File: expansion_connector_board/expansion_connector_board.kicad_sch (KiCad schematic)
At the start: 6 parts, among them J1 Conn_01x04, J12 Conn_02x17_Top_Bottom, J13 Conn_01x04, J14 Conn_02x17_Top_Bottom

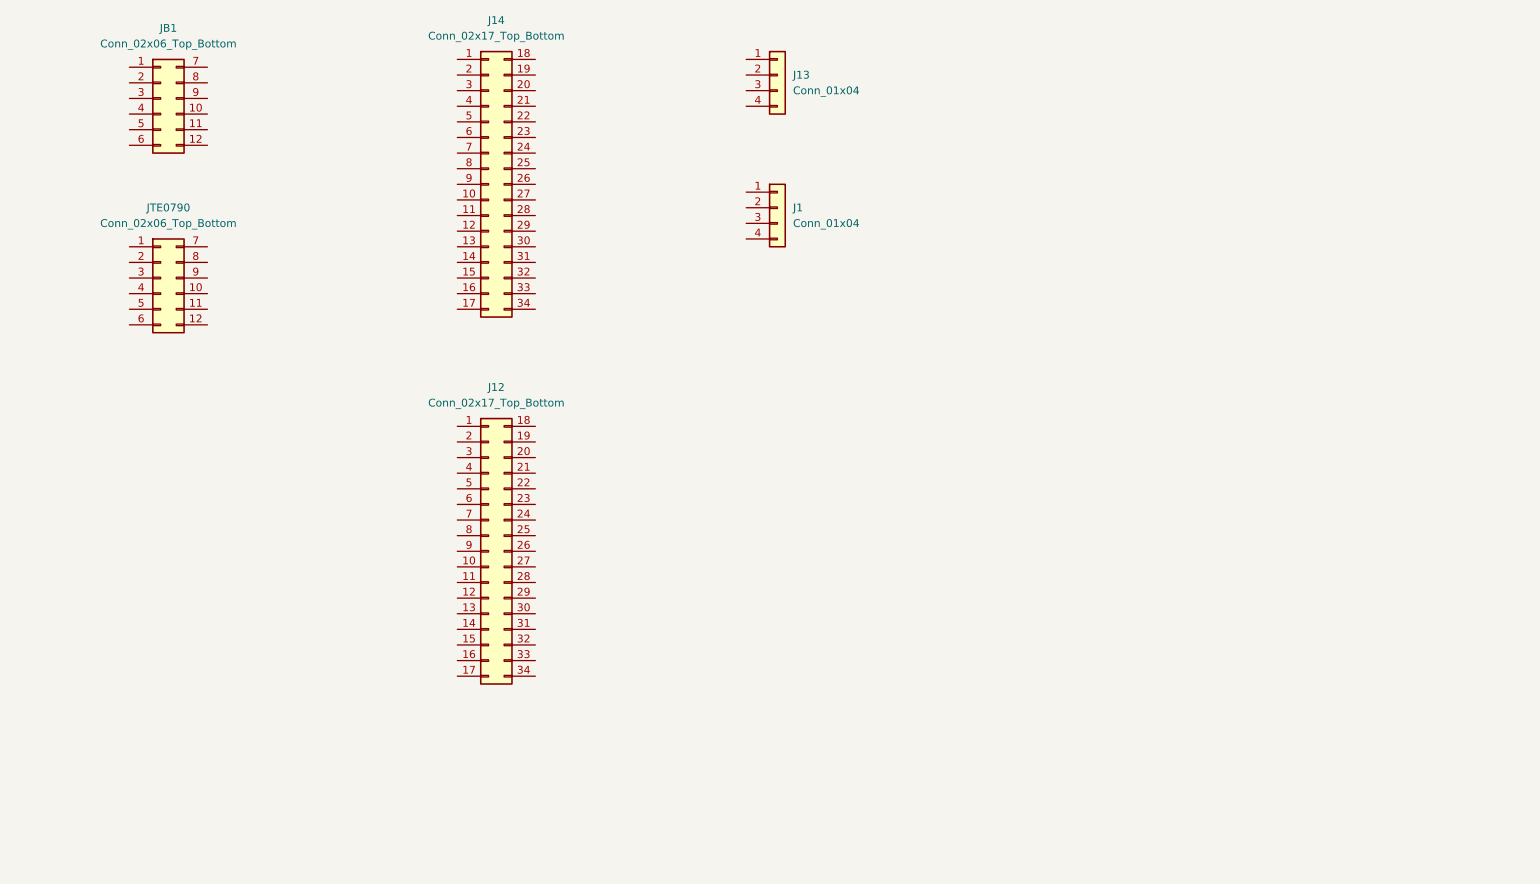
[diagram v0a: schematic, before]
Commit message: complete electrical and cutout of bridge board
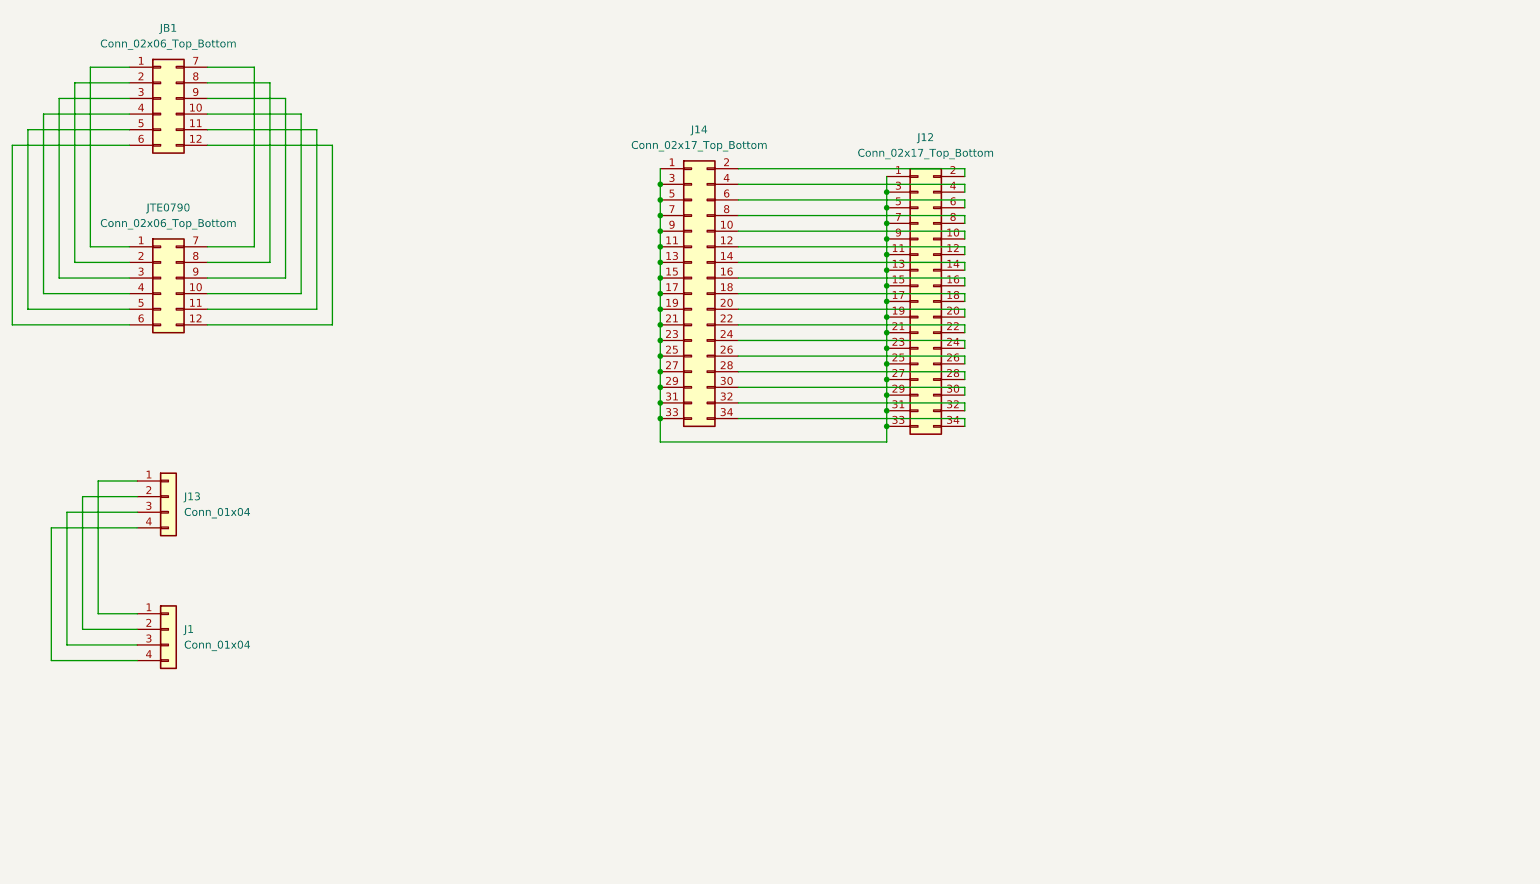
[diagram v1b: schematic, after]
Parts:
- J12, J14: symbol Connector_Generic:Conn_02x17_Top_Bottom -> Connector_Generic:Conn_02x17_Odd_Even
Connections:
- net at J12.1 (Pin_1): now also J12.11 (Pin_11), J12.13 (Pin_13), J12.15 (Pin_15), J12.17 (Pin_17), J12.19 (Pin_19), J12.21 (Pin_21), J12.23 (Pin_23), J12.25 (Pin_25), J12.27 (Pin_27), J12.29 (Pin_29), J12.3 (Pin_3), J12.31 (Pin_31), J12.33 (Pin_33), J12.5 (Pin_5), J12.7 (Pin_7), J12.9 (Pin_9), J14.1 (Pin_1), J14.11 (Pin_11), J14.13 (Pin_13), J14.15 (Pin_15), J14.17 (Pin_17), J14.19 (Pin_19), J14.21 (Pin_21), J14.23 (Pin_23), J14.25 (Pin_25), J14.27 (Pin_27), J14.29 (Pin_29), J14.3 (Pin_3), J14.31 (Pin_31), J14.33 (Pin_33), J14.5 (Pin_5), J14.7 (Pin_7), J14.9 (Pin_9)
- net at J12.10 (Pin_10): now also J14.10 (Pin_10)
- net at J12.12 (Pin_12): now also J14.12 (Pin_12)
- net at J12.14 (Pin_14): now also J14.14 (Pin_14)
- net at J12.16 (Pin_16): now also J14.16 (Pin_16)
- net at J12.18 (Pin_18): now also J14.18 (Pin_18)
- net at J12.2 (Pin_2): now also J14.2 (Pin_2)
- net at J12.20 (Pin_20): now also J14.20 (Pin_20)
- net at J12.22 (Pin_22): now also J14.22 (Pin_22)
- net at J12.24 (Pin_24): now also J14.24 (Pin_24)
- net at J12.26 (Pin_26): now also J14.26 (Pin_26)
- net at J12.28 (Pin_28): now also J14.28 (Pin_28)
- net at J12.30 (Pin_30): now also J14.30 (Pin_30)
- net at J12.32 (Pin_32): now also J14.32 (Pin_32)
- net at J12.34 (Pin_34): now also J14.34 (Pin_34)
- net at J12.4 (Pin_4): now also J14.4 (Pin_4)
- net at J12.6 (Pin_6): now also J14.6 (Pin_6)
- net at J12.8 (Pin_8): now also J14.8 (Pin_8)
- net at JB1.1 (Pin_1): now also JTE0790.1 (Pin_1)
- net at JB1.10 (Pin_10): now also JTE0790.10 (Pin_10)
- net at JB1.11 (Pin_11): now also JTE0790.11 (Pin_11)
- net at JB1.12 (Pin_12): now also JTE0790.12 (Pin_12)
- net at JB1.2 (Pin_2): now also JTE0790.2 (Pin_2)
- net at JB1.3 (Pin_3): now also JTE0790.3 (Pin_3)
- net at JB1.4 (Pin_4): now also JTE0790.4 (Pin_4)
- net at JB1.5 (Pin_5): now also JTE0790.5 (Pin_5)
- net at JB1.6 (Pin_6): now also JTE0790.6 (Pin_6)
- net at JB1.7 (Pin_7): now also JTE0790.7 (Pin_7)
- net at JB1.8 (Pin_8): now also JTE0790.8 (Pin_8)
- net at JB1.9 (Pin_9): now also JTE0790.9 (Pin_9)
- net at J13.1 (Pin_1): now also J1.1 (Pin_1)
- net at J13.2 (Pin_2): now also J1.2 (Pin_2)
- net at J13.3 (Pin_3): now also J1.3 (Pin_3)
- net at J13.4 (Pin_4): now also J1.4 (Pin_4)
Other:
- moved on the sheet: J1, J12, J13, J14

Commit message: trim board size
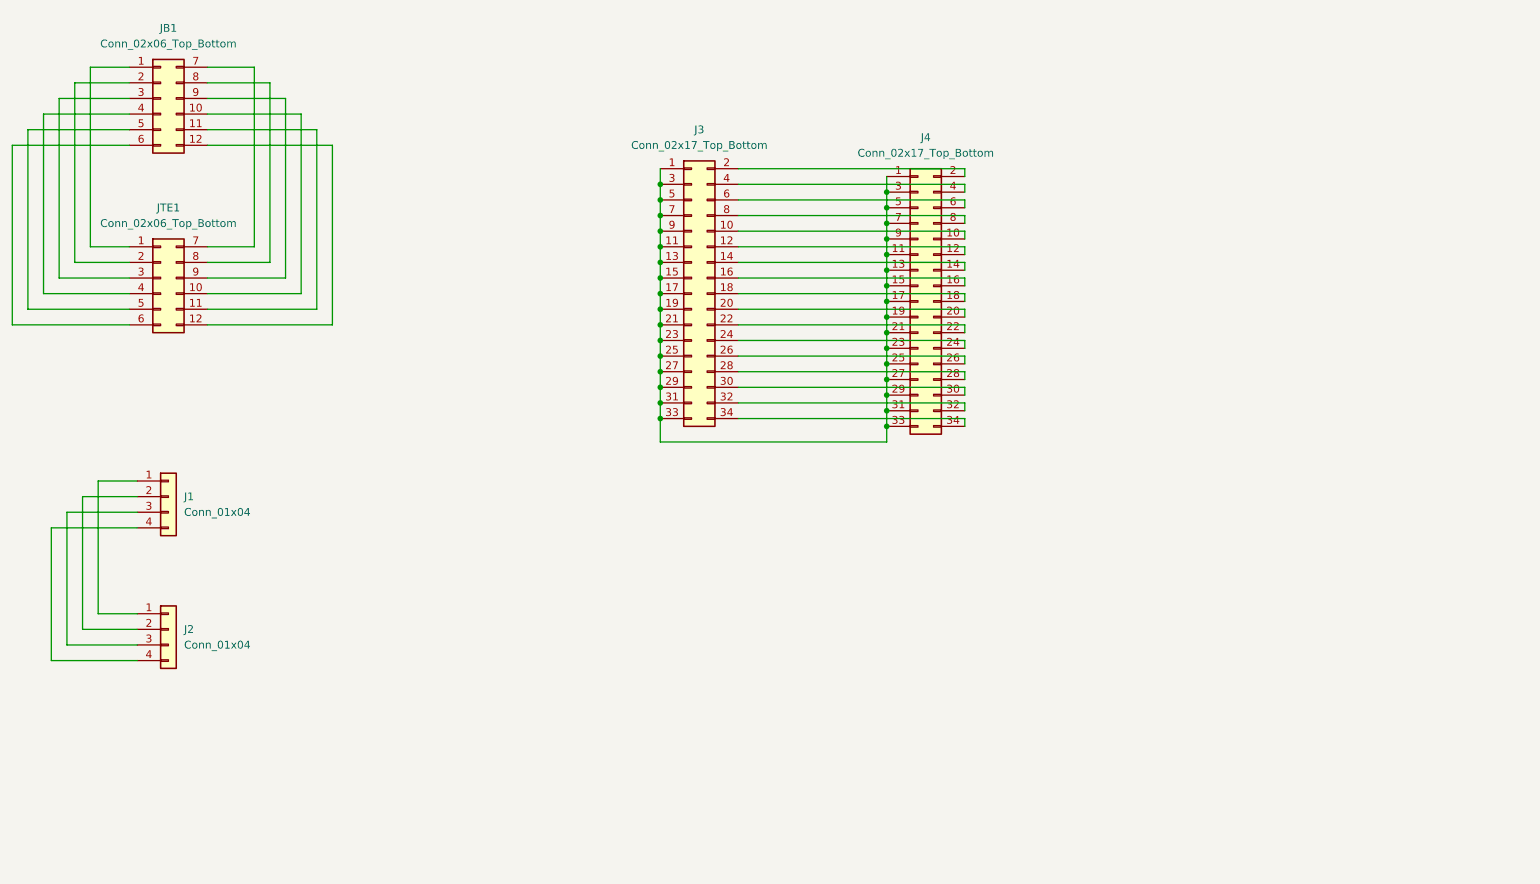
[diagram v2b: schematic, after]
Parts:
- renumbered J13 to J1, J1 to J2, J14 to J3, J12 to J4, JTE0790 to JTE1
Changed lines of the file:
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@@
   (symbol (lib_id "Connector_Generic:Conn_02x17_Odd_Even") (at 170.18 66.04 0) (unit 1)
     (in_bom yes) (on_board yes) (fields_autoplaced)
-    (property "Reference" "J12" (id 0) (at 171.45 39.37 0))
+    (property "Reference" "J4" (id 0) (at 171.45 39.37 0))
     (property "Value" "Conn_02x17_Top_Bottom" (id 1) (at 171.45 41.91 0))
     (property "Footprint" "Connector_PinHeader_2.54mm:PinHeader_2x17_P2.54mm_Vertical" (id 2) (at 170.18 66.04 0)
@@
   (symbol (lib_id "Connector_Generic:Conn_02x17_Odd_Even") (at 133.35 64.77 0) (unit 1)
     (in_bom yes) (on_board yes) (fields_autoplaced)
-    (property "Reference" "J14" (id 0) (at 134.62 38.1 0))
+    (property "Reference" "J3" (id 0) (at 134.62 38.1 0))
     (property "Value" "Conn_02x17_Top_Bottom" (id 1) (at 134.62 40.64 0))
     (property "Footprint" "Connector_PinHeader_2.54mm:PinHeader_2x17_P2.54mm_Vertical" (id 2) (at 133.35 64.77 0)
@@
   (symbol (lib_id "Connector_Generic:Conn_01x04") (at 48.26 97.79 0) (unit 1)
     (in_bom yes) (on_board yes) (fields_autoplaced)
-    (property "Reference" "J13" (id 0) (at 50.8 97.7899 0)
+    (property "Reference" "J1" (id 0) (at 50.8 97.7899 0)
       (effects (font (size 1.27 1.27)) (justify left))
     )
@@
   (symbol (lib_id "Connector_Generic:Conn_01x04") (at 48.26 119.38 0) (unit 1)
     (in_bom yes) (on_board yes) (fields_autoplaced)
-    (property "Reference" "J1" (id 0) (at 50.8 119.3799 0)
+    (property "Reference" "J2" (id 0) (at 50.8 119.3799 0)
       (effects (font (size 1.27 1.27)) (justify left))
     )
@@
   (symbol (lib_id "Connector_Generic:Conn_02x06_Top_Bottom") (at 46.99 62.23 0) (unit 1)
     (in_bom yes) (on_board yes) (fields_autoplaced)
-    (property "Reference" "JTE0790" (id 0) (at 48.26 50.8 0))
+    (property "Reference" "JTE1" (id 0) (at 48.26 50.8 0))
     (property "Value" "Conn_02x06_Top_Bottom" (id 1) (at 48.26 53.34 0))
     (property "Footprint" "Connector_PinHeader_2.54mm:PinHeader_2x06_P2.54mm_Vertical" (id 2) (at 46.99 62.23 0)
@@
   )
   (symbol_instances
-    (path "/ea63a27d-5892-4a4a-b73a-f603e7d18c36"
+    (path "/e081bfea-a76c-4079-8eff-f74da9d0a8b9"
       (reference "J1") (unit 1) (value "Conn_01x04") (footprint "Connector_PinHeader_2.54mm:PinHeader_1x04_P2.54mm_Vertical")
     )
-    (path "/4641dd2b-8a78-420d-8cf9-d253cde42a58"
-      (reference "J12") (unit 1) (value "Conn_02x17_Top_Bottom") (footprint "Connector_PinHeader_2.54mm:PinHeader_2x17_P2.54mm_Vertical")
-    )
-    (path "/e081bfea-a76c-4079-8eff-f74da9d0a8b9"
-      (reference "J13") (unit 1) (value "Conn_01x04") (footprint "Connector_PinHeader_2.54mm:PinHeader_1x04_P2.54mm_Vertical")
+    (path "/ea63a27d-5892-4a4a-b73a-f603e7d18c36"
+      (reference "J2") (unit 1) (value "Conn_01x04") (footprint "Connector_PinHeader_2.54mm:PinHeader_1x04_P2.54mm_Vertical")
     )
     (path "/5e2b1b60-5db0-4075-8d2c-1c593da01486"
-      (reference "J14") (unit 1) (value "Conn_02x17_Top_Bottom") (footprint "Connector_PinHeader_2.54mm:PinHeader_2x17_P2.54mm_Vertical")
+      (reference "J3") (unit 1) (value "Conn_02x17_Top_Bottom") (footprint "Connector_PinHeader_2.54mm:PinHeader_2x17_P2.54mm_Vertical")
+    )
+    (path "/4641dd2b-8a78-420d-8cf9-d253cde42a58"
+      (reference "J4") (unit 1) (value "Conn_02x17_Top_Bottom") (footprint "Connector_PinHeader_2.54mm:PinHeader_2x17_P2.54mm_Vertical")
     )
     (path "/db6f34f2-3650-4262-8a8c-0ff568fe194f"
@@
     )
     (path "/f61065d3-62f3-4952-9f93-3fd8792c420d"
-      (reference "JTE0790") (unit 1) (value "Conn_02x06_Top_Bottom") (footprint "Connector_PinHeader_2.54mm:PinHeader_2x06_P2.54mm_Vertical")
+      (reference "JTE1") (unit 1) (value "Conn_02x06_Top_Bottom") (footprint "Connector_PinHeader_2.54mm:PinHeader_2x06_P2.54mm_Vertical")
     )
   )

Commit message: fix connector placement on bridge board
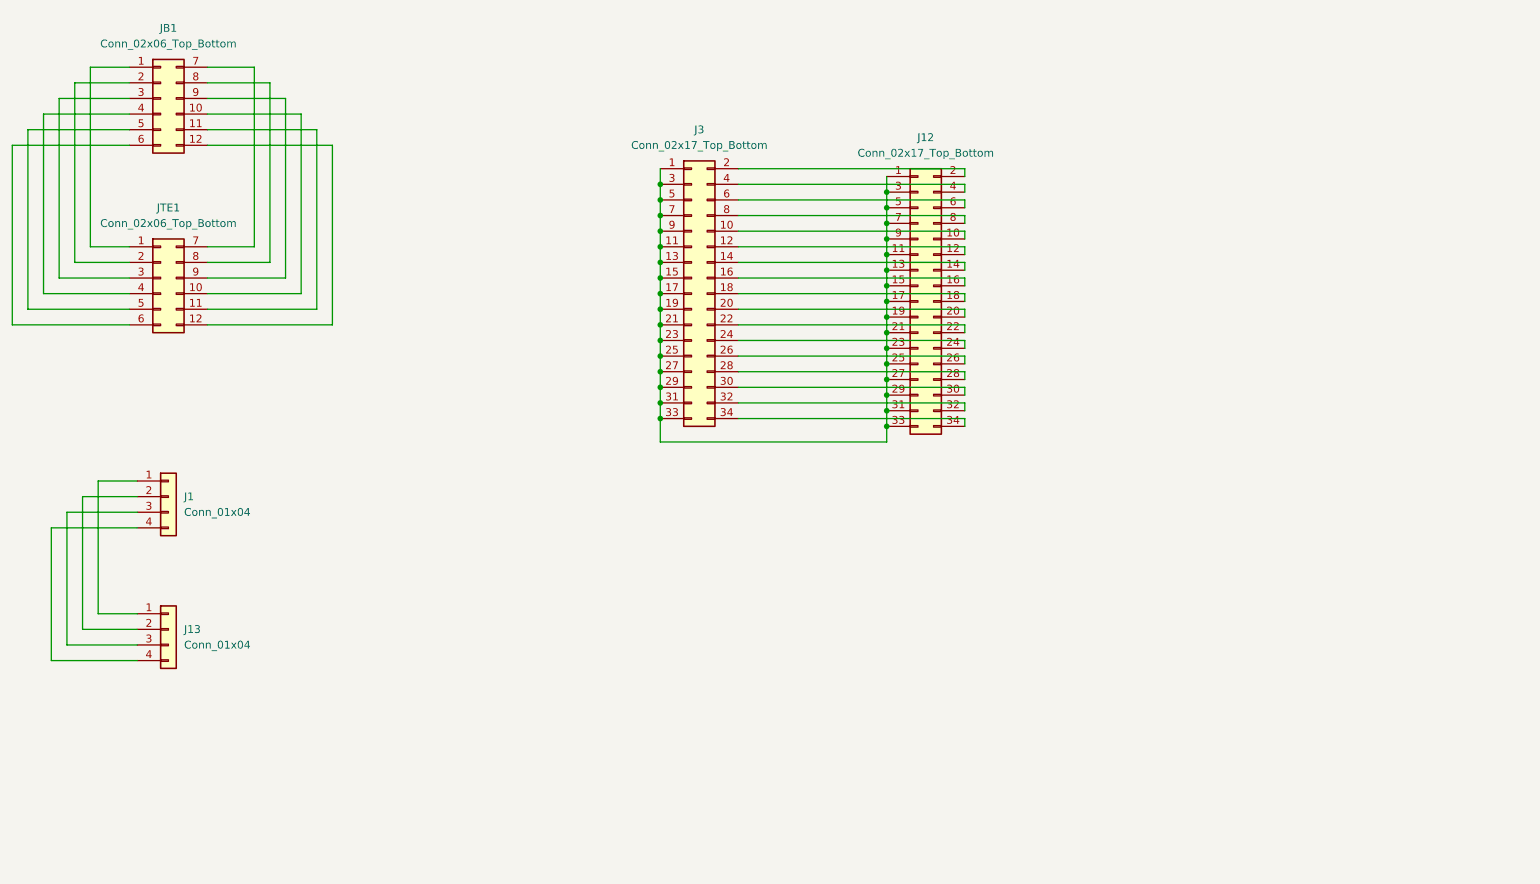
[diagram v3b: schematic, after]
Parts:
- renumbered J4 to J12, J2 to J13
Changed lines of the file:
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@@
   (symbol (lib_id "Connector_Generic:Conn_02x17_Odd_Even") (at 170.18 66.04 0) (unit 1)
     (in_bom yes) (on_board yes) (fields_autoplaced)
-    (property "Reference" "J4" (id 0) (at 171.45 39.37 0))
+    (property "Reference" "J12" (id 0) (at 171.45 39.37 0))
     (property "Value" "Conn_02x17_Top_Bottom" (id 1) (at 171.45 41.91 0))
     (property "Footprint" "Connector_PinHeader_2.54mm:PinHeader_2x17_P2.54mm_Vertical" (id 2) (at 170.18 66.04 0)
@@
   (symbol (lib_id "Connector_Generic:Conn_01x04") (at 48.26 119.38 0) (unit 1)
     (in_bom yes) (on_board yes) (fields_autoplaced)
-    (property "Reference" "J2" (id 0) (at 50.8 119.3799 0)
+    (property "Reference" "J13" (id 0) (at 50.8 119.3799 0)
       (effects (font (size 1.27 1.27)) (justify left))
     )
@@
       (reference "J1") (unit 1) (value "Conn_01x04") (footprint "Connector_PinHeader_2.54mm:PinHeader_1x04_P2.54mm_Vertical")
     )
-    (path "/ea63a27d-5892-4a4a-b73a-f603e7d18c36"
-      (reference "J2") (unit 1) (value "Conn_01x04") (footprint "Connector_PinHeader_2.54mm:PinHeader_1x04_P2.54mm_Vertical")
-    )
     (path "/5e2b1b60-5db0-4075-8d2c-1c593da01486"
       (reference "J3") (unit 1) (value "Conn_02x17_Top_Bottom") (footprint "Connector_PinHeader_2.54mm:PinHeader_2x17_P2.54mm_Vertical")
     )
     (path "/4641dd2b-8a78-420d-8cf9-d253cde42a58"
-      (reference "J4") (unit 1) (value "Conn_02x17_Top_Bottom") (footprint "Connector_PinHeader_2.54mm:PinHeader_2x17_P2.54mm_Vertical")
+      (reference "J12") (unit 1) (value "Conn_02x17_Top_Bottom") (footprint "Connector_PinHeader_2.54mm:PinHeader_2x17_P2.54mm_Vertical")
+    )
+    (path "/ea63a27d-5892-4a4a-b73a-f603e7d18c36"
+      (reference "J13") (unit 1) (value "Conn_01x04") (footprint "Connector_PinHeader_2.54mm:PinHeader_1x04_P2.54mm_Vertical")
     )
     (path "/db6f34f2-3650-4262-8a8c-0ff568fe194f"

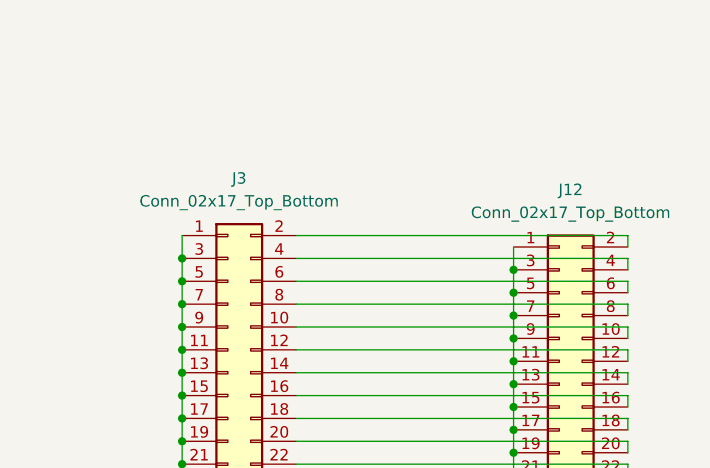
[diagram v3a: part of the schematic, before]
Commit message: fill-out size of bridge board to fit wifi etc
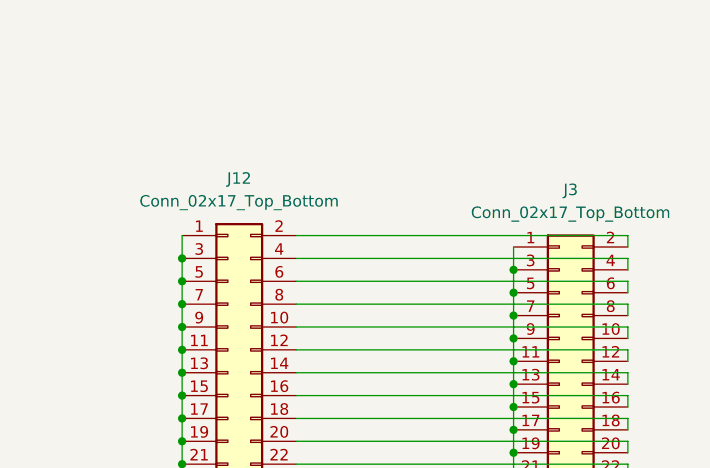
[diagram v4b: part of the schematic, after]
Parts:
- renumbered J3 to J12, J12 to J3
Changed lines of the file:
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@@
   (symbol (lib_id "Connector_Generic:Conn_02x17_Odd_Even") (at 170.18 66.04 0) (unit 1)
     (in_bom yes) (on_board yes) (fields_autoplaced)
-    (property "Reference" "J12" (id 0) (at 171.45 39.37 0))
+    (property "Reference" "J3" (id 0) (at 171.45 39.37 0))
     (property "Value" "Conn_02x17_Top_Bottom" (id 1) (at 171.45 41.91 0))
     (property "Footprint" "Connector_PinHeader_2.54mm:PinHeader_2x17_P2.54mm_Vertical" (id 2) (at 170.18 66.04 0)
@@
   (symbol (lib_id "Connector_Generic:Conn_02x17_Odd_Even") (at 133.35 64.77 0) (unit 1)
     (in_bom yes) (on_board yes) (fields_autoplaced)
-    (property "Reference" "J3" (id 0) (at 134.62 38.1 0))
+    (property "Reference" "J12" (id 0) (at 134.62 38.1 0))
     (property "Value" "Conn_02x17_Top_Bottom" (id 1) (at 134.62 40.64 0))
     (property "Footprint" "Connector_PinHeader_2.54mm:PinHeader_2x17_P2.54mm_Vertical" (id 2) (at 133.35 64.77 0)
@@
       (reference "J1") (unit 1) (value "Conn_01x04") (footprint "Connector_PinHeader_2.54mm:PinHeader_1x04_P2.54mm_Vertical")
     )
-    (path "/5e2b1b60-5db0-4075-8d2c-1c593da01486"
+    (path "/4641dd2b-8a78-420d-8cf9-d253cde42a58"
       (reference "J3") (unit 1) (value "Conn_02x17_Top_Bottom") (footprint "Connector_PinHeader_2.54mm:PinHeader_2x17_P2.54mm_Vertical")
     )
-    (path "/4641dd2b-8a78-420d-8cf9-d253cde42a58"
+    (path "/5e2b1b60-5db0-4075-8d2c-1c593da01486"
       (reference "J12") (unit 1) (value "Conn_02x17_Top_Bottom") (footprint "Connector_PinHeader_2.54mm:PinHeader_2x17_P2.54mm_Vertical")
     )
